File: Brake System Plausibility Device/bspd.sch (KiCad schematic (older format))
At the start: 34 parts, among them P1 MX150_16, U1 MCP604, U2 LM1117-5.0, U3 74LVC2G74, U4 74AUC2G00

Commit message: Decoupling caps annotated
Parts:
- gave numbers to parts that had none: 8
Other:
- note added: "Opamp Decoupling"

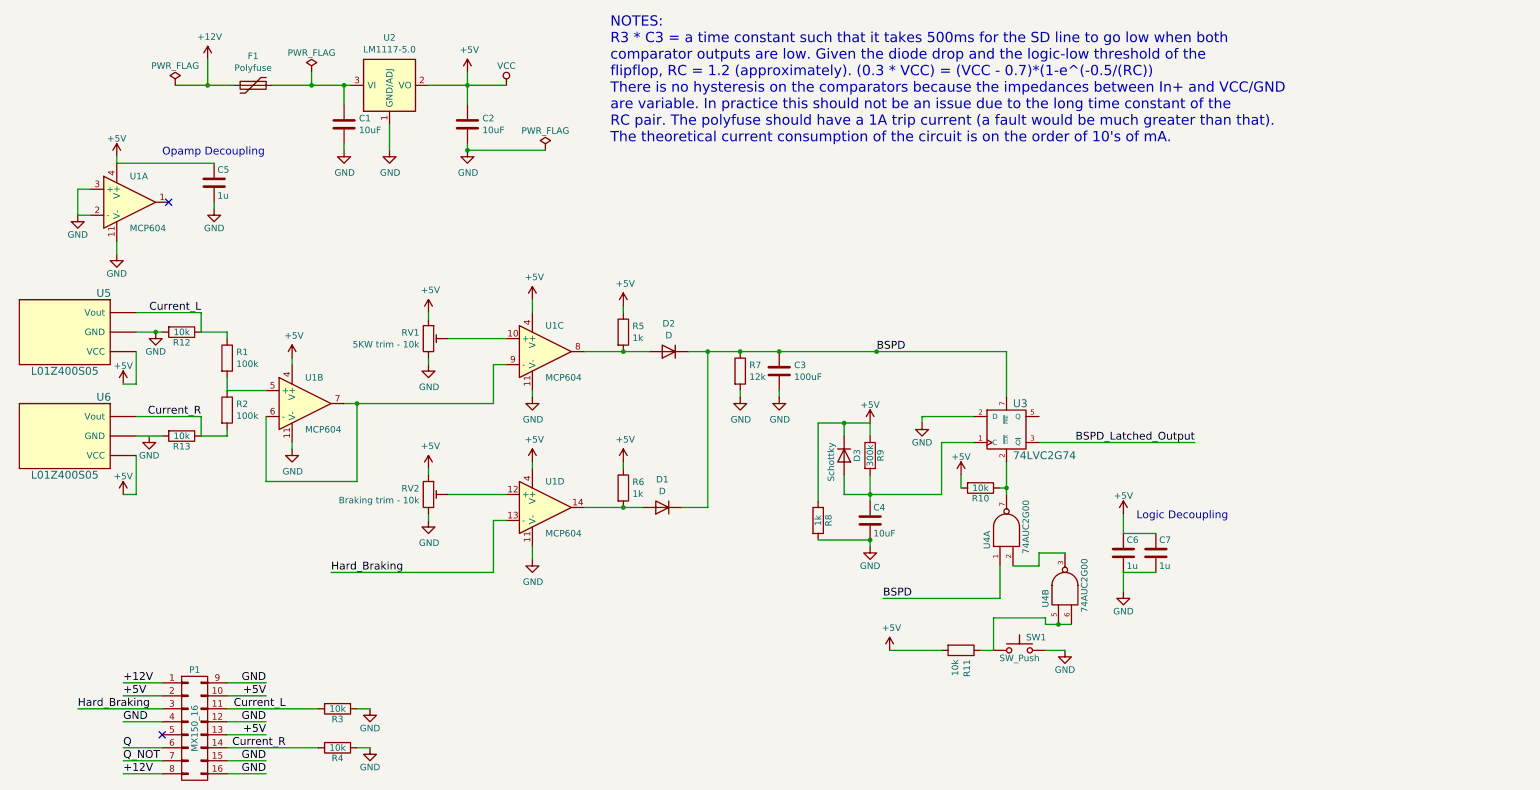
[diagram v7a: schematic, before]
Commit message: Decoupling updates, small VCU changes
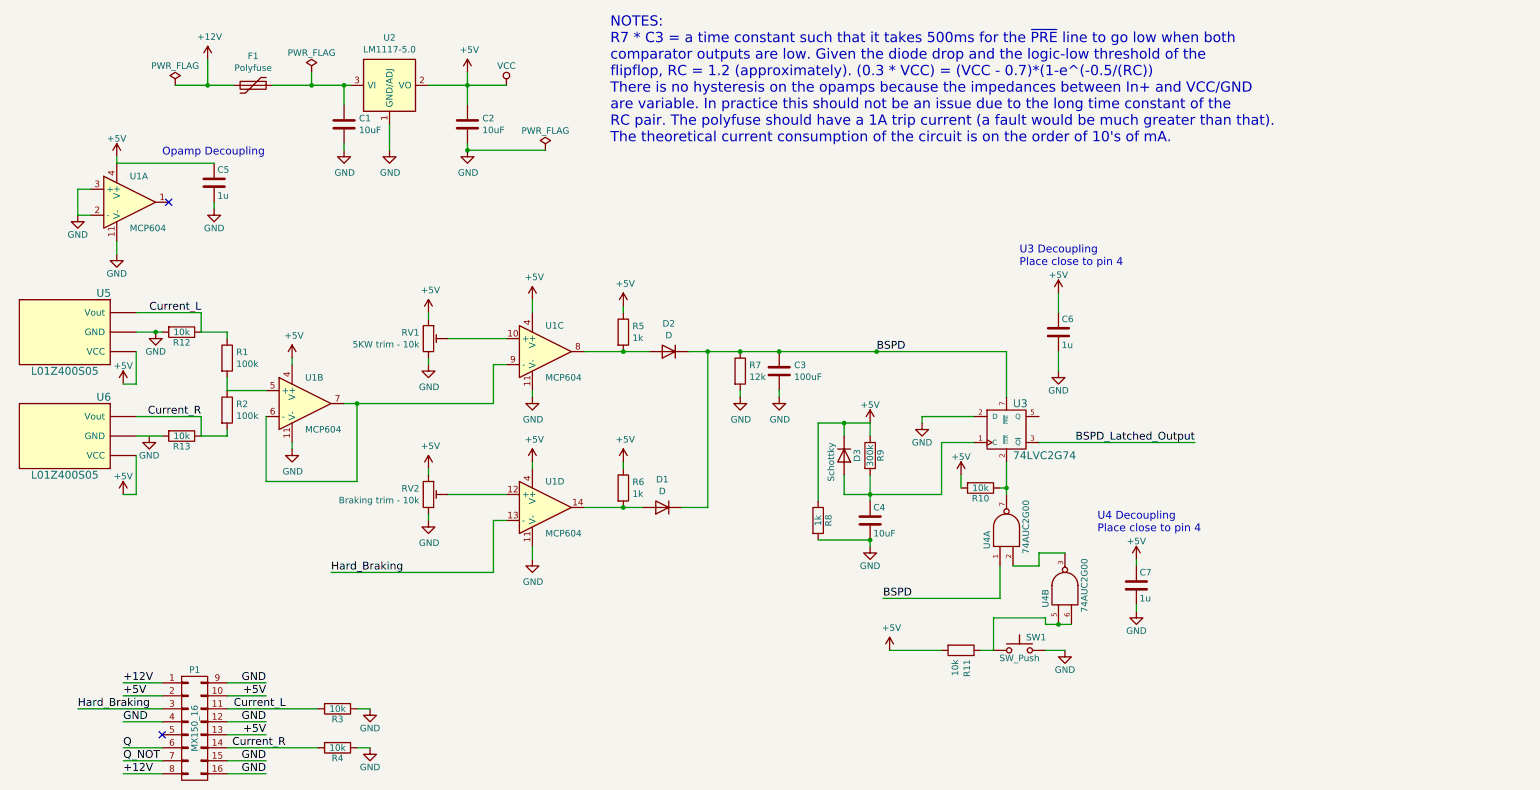
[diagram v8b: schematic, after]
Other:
- note added: "NOTES:\nR7 * C3 = a time constant such that it takes 500ms for the ~PRE~ line to go low when both \ncomparator outputs are low. Given the diode drop and the logic-low threshold of the \nflipflop, RC = 1.2 (approximately). (0.3 * VCC) = (VCC - 0.7)*(1-e^(-0.5/(RC))\nThere is no hysteresis on the opamps because the impedances between In+ and VCC/GND\nare variable. In practice this should not be an 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"
- note added: "U3 Decoupling\nPlace close to pin 4"
- note added: "U4 Decoupling\nPlace close to pin 4\n"
- note removed: "Logic Decoupling\n"
- note removed: "NOTES:\nR3 * C3 = a time constant such that it takes 500ms for the SD line to go low when both \ncomparator outputs are low. Given the diode drop and the logic-low threshold of the \nflipflop, RC = 1.2 (approximately). (0.3 * VCC) = (VCC - 0.7)*(1-e^(-0.5/(RC))\nThere is no hysteresis on the comparators because the impedances between In+ and VCC/GND\nare variable. In practice this should not be a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"
- moved on the sheet: C6, C7
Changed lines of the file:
@@
 Connection ~ 3050 1050
 Text Notes 5100 1500 0    79   ~ 0
-NOTES:\nR3 * C3 = a time constant such that it takes 500ms for the SD line to go low when both \ncomparator outputs are low. Given the diode drop and the logic-low threshold of the \nflipflop, RC = 1.2 (approximately). (0.3 * VCC) = (VCC - 0.7)*(1-e^(-0.5/(RC))\nThere is no hysteresis on the comparators because the impedances between In+ and VCC/GND\nare variable. In practice this should not be an issue due to the long time constant of the \nRC pair. The polyfuse should have a 1A trip current (a fault would be much greater than that). \nThe theoretical current consumption of the circuit is on the order of 10's of mA.
+NOTES:\nR7 * C3 = a time constant such that it takes 500ms for the ~PRE~ line to go low when both \ncomparator outputs are low. Given the diode drop and the logic-low threshold of the \nflipflop, RC = 1.2 (approximately). (0.3 * VCC) = (VCC - 0.7)*(1-e^(-0.5/(RC))\nThere is no hysteresis on the opamps because the impedances between In+ and VCC/GND\nare variable. In practice this should not be an issue due to the long time constant of the \nRC pair. The polyfuse should have a 1A trip current (a fault would be much greater than that). \nThe theoretical current consumption of the circuit is on the order of 10's of mA.
 Wire Wire Line
 	5700 3100 8150 3100
@@
 L C C6
 U 1 1 58D05677
-P 9050 4650
-F 0 "C6" H 9075 4750 50  0000 L CNN
-F 1 "1u" H 9075 4550 50  0000 L CNN
-F 2 "" H 9088 4500 50  0001 C CNN
-F 3 "" H 9050 4650 50  0001 C CNN
-	1    9050 4650
+P 8550 2950
+F 0 "C6" H 8575 3050 50  0000 L CNN
+F 1 "1u" H 8575 2850 50  0000 L CNN
+F 2 "" H 8588 2800 50  0001 C CNN
+F 3 "" H 8550 2950 50  0001 C CNN
+	1    8550 2950
 	1    0    0    -1
 $EndComp
@@
 L C C7
 U 1 1 58D056FA
-P 9300 4650
-F 0 "C7" H 9325 4750 50  0000 L CNN
-F 1 "1u" H 9325 4550 50  0000 L CNN
-F 2 "" H 9338 4500 50  0001 C CNN
-F 3 "" H 9300 4650 50  0001 C CNN
-	1    9300 4650
+P 9150 4900
+F 0 "C7" H 9175 5000 50  0000 L CNN
+F 1 "1u" H 9175 4800 50  0000 L CNN
+F 2 "" H 9188 4750 50  0001 C CNN
+F 3 "" H 9150 4900 50  0001 C CNN
+	1    9150 4900
 	1    0    0    -1
 $EndComp
@@
 L +5V #PWR37
 U 1 1 58D05BAC
-P 9050 4350
-F 0 "#PWR37" H 9050 4200 50  0001 C CNN
-F 1 "+5V" H 9050 4490 50  0000 C CNN
-F 2 "" H 9050 4350 50  0001 C CNN
-F 3 "" H 9050 4350 50  0001 C CNN
-	1    9050 4350
+P 8550 2650
+F 0 "#PWR37" H 8550 2500 50  0001 C CNN
+F 1 "+5V" H 8550 2790 50  0000 C CNN
+F 2 "" H 8550 2650 50  0001 C CNN
+F 3 "" H 8550 2650 50  0001 C CNN
+	1    8550 2650
 	1    0    0    -1
 $EndComp
@@
 L GND #PWR38
 U 1 1 58D05C08
-P 9050 4950
-F 0 "#PWR38" H 9050 4700 50  0001 C CNN
-F 1 "GND" H 9050 4800 50  0000 C CNN
-F 2 "" H 9050 4950 50  0001 C CNN
-F 3 "" H 9050 4950 50  0001 C CNN
-	1    9050 4950
-	1    0    0    -1
-$EndComp
-Wire Wire Line
-	9050 4950 9050 4800
-Wire Wire Line
-	9050 4800 9300 4800
-Wire Wire Line
-	9300 4500 9050 4500
-Wire Wire Line
-	9050 4500 9050 4350
-Text Notes 9150 4400 0    60   ~ 0
-Logic Decoupling\n
+P 8550 3250
+F 0 "#PWR38" H 8550 3000 50  0001 C CNN
+F 1 "GND" H 8550 3100 50  0000 C CNN
+F 2 "" H 8550 3250 50  0001 C CNN
+F 3 "" H 8550 3250 50  0001 C CNN
+	1    8550 3250
+	1    0    0    -1
+$EndComp
+Wire Wire Line
+	8550 3250 8550 3100
+Wire Wire Line
+	8550 2800 8550 2650
 $Comp
 L L01Z400S05 U5
@@
 Text Notes 1650 1600 0    60   ~ 0
 Opamp Decoupling
+Text Notes 8250 2450 0    60   ~ 0
+U3 Decoupling\nPlace close to pin 4
+$Comp
+L +5V #PWR?
+U 1 1 59093498
+P 9150 4700
+F 0 "#PWR?" H 9150 4550 50  0001 C CNN
+F 1 "+5V" H 9150 4840 50  0000 C CNN
+F 2 "" H 9150 4700 50  0001 C CNN
+F 3 "" H 9150 4700 50  0001 C CNN
+	1    9150 4700
+	1    0    0    -1
+$EndComp
+Wire Wire Line
+	9150 4700 9150 4750
+$Comp
+L GND #PWR?
+U 1 1 590935A3
+P 9150 5100
+F 0 "#PWR?" H 9150 4850 50  0001 C CNN
+F 1 "GND" H 9150 4950 50  0000 C CNN
+F 2 "" H 9150 5100 50  0001 C CNN
+F 3 "" H 9150 5100 50  0001 C CNN
+	1    9150 5100
+	1    0    0    -1
+$EndComp
+Wire Wire Line
+	9150 5100 9150 5050
+Text Notes 8850 4500 0    60   ~ 0
+U4 Decoupling\nPlace close to pin 4\n
 $EndSCHEMATC
